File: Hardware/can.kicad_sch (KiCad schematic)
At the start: 9 parts, among them U2 SN65HVD230

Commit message: Finished Boosts and Sensors
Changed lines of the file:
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@@
 (kicad_sch
-	(version 20231120)
+	(version 20250114)
 	(generator "eeschema")
-	(generator_version "8.0")
+	(generator_version "9.0")
 	(paper "A4")
 	(junction
@@
 	(label "Vref"
 		(at 124.46 90.17 180)
-		(fields_autoplaced yes)
 		(effects
 			(font
@@
 	(label "Vref"
 		(at 153.67 88.9 180)
-		(fields_autoplaced yes)
 		(effects
 			(font
@@
 		(shape input)
 		(at 111.76 87.63 180)
-		(fields_autoplaced yes)
 		(effects
 			(font
@@
 		(shape bidirectional)
 		(at 175.26 80.01 0)
-		(fields_autoplaced yes)
 		(effects
 			(font
@@
 		(shape output)
 		(at 111.76 85.09 180)
-		(fields_autoplaced yes)
 		(effects
 			(font
@@
 		(shape bidirectional)
 		(at 190.5 97.79 0)
-		(fields_autoplaced yes)
 		(effects
 			(font
@@
 		(shape bidirectional)
 		(at 190.5 80.01 0)
-		(fields_autoplaced yes)
 		(effects
 			(font
@@
 		(shape bidirectional)
 		(at 175.26 97.79 0)
-		(fields_autoplaced yes)
-		(effects
-			(font
+		(effects
+			(font

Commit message: Almost done
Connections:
- net CAN_HIGH: now also D1.1 (A1); no longer D1.2 (A2)
- net CAN_LOW: now also D1.2 (A2); no longer D1.1 (A1)
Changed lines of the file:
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@@
 	(hierarchical_label "CAN_HIGH"
 		(shape bidirectional)
-		(at 190.5 97.79 0)
+		(at 190.5 80.01 0)
 		(effects
 			(font
@@
 	(hierarchical_label "CAN_LOW"
 		(shape bidirectional)
-		(at 190.5 80.01 0)
+		(at 190.5 97.79 0)
 		(effects
 			(font

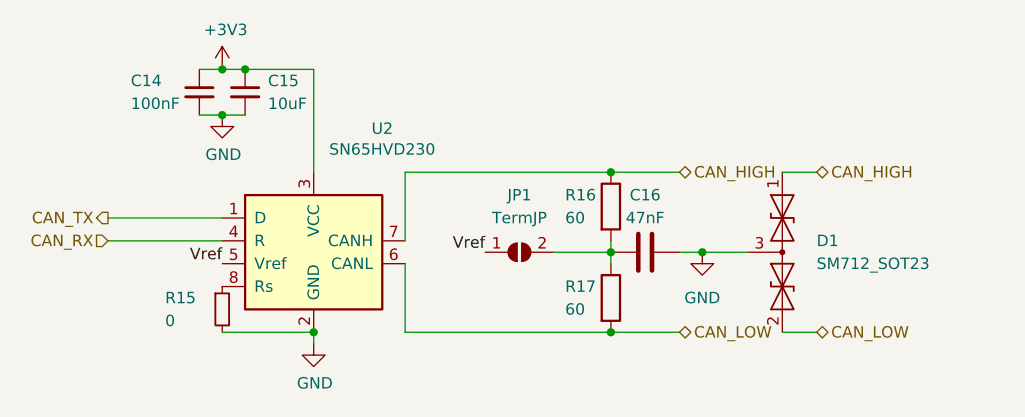
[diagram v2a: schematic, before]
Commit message: can termination upgrade
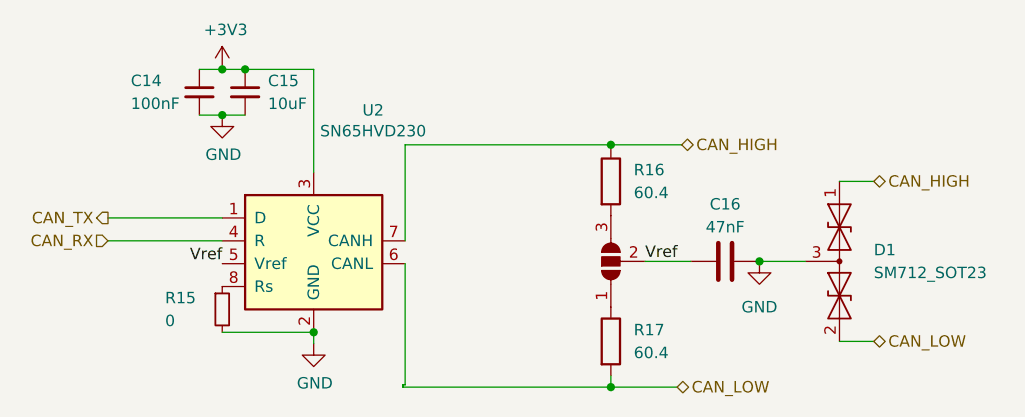
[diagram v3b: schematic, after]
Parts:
- removed JP1: TermJP, iclr:SmallerSolderJP, symbol Jumper:SolderJumper_2_Open
- added JP30: SolderJumper_3_Open, iclr:small_3pin_SolderJP, symbol Jumper:SolderJumper_3_Open
- R15: footprint Resistor_SMD:R_0603_1608Metric -> Resistor_SMD:R_0402_1005Metric
- R16, R17: value 60 -> 60.4; footprint Resistor_SMD:R_0603_1608Metric -> Resistor_SMD:R_0402_1005Metric
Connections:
- net Vref: now also C16.1, JP30.2 (C)
- new net: JP30.1 (A), R17.1
- new net: JP30.3 (B), R16.2
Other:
- moved on the sheet: C16, D1, R16, R17

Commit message: schematic reformatting and bom consolidation
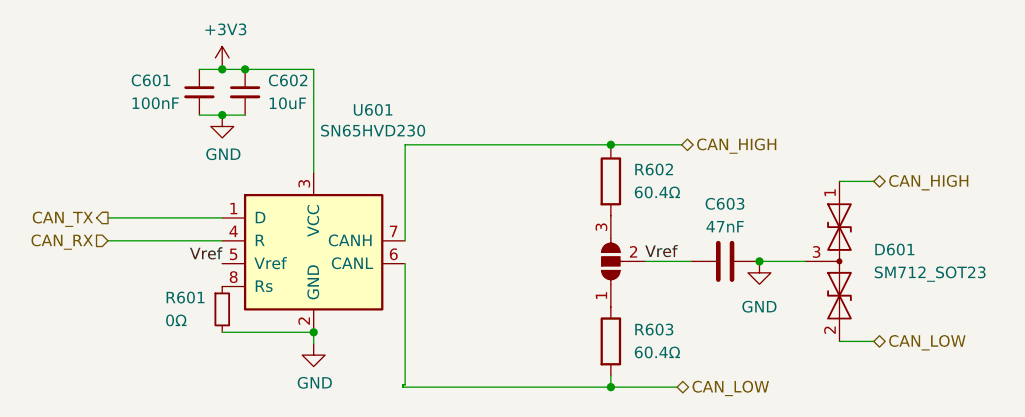
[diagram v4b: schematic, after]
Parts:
- JP601: renamed from JP30; now left out of the parts list
- R601: renamed from R15; value 0 -> 0Ω
- R602: renamed from R16; value 60.4 -> 60.4Ω
- R603: renamed from R17; value 60.4 -> 60.4Ω
- renumbered C14 to C601, C15 to C602, C16 to C603, D1 to D601, U2 to U601
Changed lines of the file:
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@@
 		(dnp no)
 		(fields_autoplaced yes)
-		(property "Reference" "#PWR035"
+		(property "Reference" "#PWR0603"
 			(at 134.62 105.41 0)
 			(effects
@@
 			(project "Ricardo-Stark"
 				(path "/7db990e4-92e1-4f99-b4d2-435bbec1ba83/00000000-0000-0000-0000-000061942b9a"
-					(reference "#PWR035")
+					(reference "#PWR0603")
 					(unit 1)
 				)
@@
 		(dnp no)
 		(fields_autoplaced yes)
-		(property "Reference" "#PWR033"
+		(property "Reference" "#PWR0601"
 			(at 124.46 72.39 0)
 			(effects
@@
 			(project "Ricardo-Stark"
 				(path "/7db990e4-92e1-4f99-b4d2-435bbec1ba83/00000000-0000-0000-0000-000061942b9a"
-					(reference "#PWR033")
+					(reference "#PWR0601")
 					(unit 1)
 				)
@@
 		(on_board yes)
 		(dnp no)
-		(property "Reference" "U2"
+		(property "Reference" "U601"
 			(at 141.224 73.1266 0)
 			(effects
@@
 			(project "Ricardo-Stark"
 				(path "/7db990e4-92e1-4f99-b4d2-435bbec1ba83/00000000-0000-0000-0000-000061942b9a"
-					(reference "U2")
+					(reference "U601")
 					(unit 1)
 				)
@@
 		(dnp no)
 		(fields_autoplaced yes)
-		(property "Reference" "C15"
+		(property "Reference" "C602"
 			(at 129.54 69.8562 0)
 			(effects
@@
 			(project "Ricardo-Stark"
 				(path "/7db990e4-92e1-4f99-b4d2-435bbec1ba83/00000000-0000-0000-0000-000061942b9a"
-					(reference "C15")
+					(reference "C602")
 					(unit 1)
 				)
@@
 		(dnp no)
 		(fields_autoplaced yes)
-		(property "Reference" "D1"
+		(property "Reference" "D601"
 			(at 196.85 88.646 90)
 			(effects
@@
 			(project "Ricardo-Stark"
 				(path "/7db990e4-92e1-4f99-b4d2-435bbec1ba83/00000000-0000-0000-0000-000061942b9a"
-					(reference "D1")
+					(reference "D601")
 					(unit 1)
 				)
@@
 		(dnp no)
 		(fields_autoplaced yes)
-		(property "Reference" "#PWR036"
+		(property "Reference" "#PWR0604"
 			(at 184.15 96.266 0)
 			(effects
@@
 			(project "Ricardo-Stark"
 				(path "/7db990e4-92e1-4f99-b4d2-435bbec1ba83/00000000-0000-0000-0000-000061942b9a"
-					(reference "#PWR036")
+					(reference "#PWR0604")
 					(unit 1)
 				)
@@
 		(dnp no)
 		(fields_autoplaced yes)
-		(property "Reference" "C14"
+		(property "Reference" "C601"
 			(at 114.3 69.85 0)
 			(effects
@@
 			(project "Ricardo-Stark"
 				(path "/7db990e4-92e1-4f99-b4d2-435bbec1ba83/00000000-0000-0000-0000-000061942b9a"
-					(reference "C14")
+					(reference "C601")
 					(unit 1)
 				)
@@
 		(unit 1)
 		(exclude_from_sim no)
-		(in_bom yes)
-		(on_board yes)
-		(dnp no)
-		(property "Reference" "JP30"
+		(in_bom no)
+		(on_board yes)
+		(dnp no)
+		(property "Reference" "JP601"
 			(at 165.1 88.646 90)
 			(effects
@@
 			(project "Ricardo-Stark"
 				(path "/7db990e4-92e1-4f99-b4d2-435bbec1ba83/00000000-0000-0000-0000-000061942b9a"
-					(reference "JP30")
+					(reference "JP601")
 					(unit 1)
 				)
@@
 		(on_board yes)
 		(dnp no)
-		(property "Reference" "R15"
+		(property "Reference" "R601"
 			(at 118.11 93.98 0)
 			(effects
@@
 			)
 		)
-		(property "Value" "0"
+		(property "Value" "0Ω"
 			(at 118.11 96.52 0)
 			(effects
@@
 			(project "Ricardo-Stark"
 				(path "/7db990e4-92e1-4f99-b4d2-435bbec1ba83/00000000-0000-0000-0000-000061942b9a"
-					(reference "R15")
+					(reference "R601")
 					(unit 1)
 				)
@@
 		(dnp no)
 		(fields_autoplaced yes)
-		(property "Reference" "R17"
+		(property "Reference" "R603"
 			(at 170.18 97.5359 0)
 			(effects
@@
 			)
 		)
-		(property "Value" "60.4"
+		(property "Value" "60.4Ω"
 			(at 170.18 100.0759 0)
 			(effects
@@
 			(project "Ricardo-Stark"
 				(path "/7db990e4-92e1-4f99-b4d2-435bbec1ba83/00000000-0000-0000-0000-000061942b9a"
-					(reference "R17")
+					(reference "R603")
 					(unit 1)
 				)
@@
 		(dnp no)
 		(fields_autoplaced yes)
-		(property "Reference" "R16"
+		(property "Reference" "R602"
 			(at 170.18 79.7559 0)
 			(effects
@@
 			)
 		)
-		(property "Value" "60.4"
+		(property "Value" "60.4Ω"
 			(at 170.18 82.2959 0)
 			(effects
@@
 			(project "Ricardo-Stark"
 				(path "/7db990e4-92e1-4f99-b4d2-435bbec1ba83/00000000-0000-0000-0000-000061942b9a"
-					(reference "R16")
+					(reference "R602")
 					(unit 1)
 				)
@@
 		(dnp no)
 		(fields_autoplaced yes)
-		(property "Reference" "C16"
+		(property "Reference" "C603"
 			(at 180.34 83.566 90)
 			(effects
@@
 			(project "Ricardo-Stark"
 				(path "/7db990e4-92e1-4f99-b4d2-435bbec1ba83/00000000-0000-0000-0000-000061942b9a"
-					(reference "C16")
+					(reference "C603")
 					(unit 1)
 				)
@@
 		(dnp no)
 		(fields_autoplaced yes)
-		(property "Reference" "#PWR034"
+		(property "Reference" "#PWR0602"
 			(at 124.46 80.01 0)
 			(effects
@@
 			(project "Ricardo-Stark"
 				(path "/7db990e4-92e1-4f99-b4d2-435bbec1ba83/00000000-0000-0000-0000-000061942b9a"
-					(reference "#PWR034")
-					(unit 1)
-				)
+					(reference "#PWR0602")
+					(unit 1)
+				)
